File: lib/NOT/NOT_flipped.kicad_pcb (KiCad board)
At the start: 2 copper layers, 2 parts, among them P1 Q_PJFET_GSD

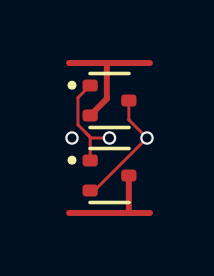
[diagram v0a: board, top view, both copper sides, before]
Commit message: The layout of the NOT gate was also botched (PMOS pinout wrong)
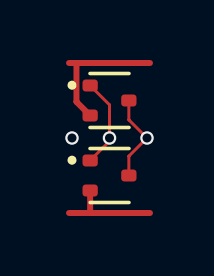
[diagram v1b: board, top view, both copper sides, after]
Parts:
- N1: value Q_NJFET_GSD -> (none)
- P1: value Q_PJFET_GSD -> (none)
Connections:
- P1 pad 2: Y -> VDD
- P1 pad 3: VDD -> Y
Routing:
- net Y: track 4.12 -> 3.00 mm
- net A: track 3.65 -> 3.03 mm
- net VDD: track 3.95 -> 3.45 mm
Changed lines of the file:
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@@
 			)
 		)
-		(property "Value" "Q_PJFET_GSD"
+		(property "Value" ""
 			(at 0 1.75 0)
 			(layer "F.Fab")
@@
 			)
 		)
-		(sheetname "/")
-		(sheetfile "NOT.kicad_sch")
 		(attr smd)
 		(fp_line
@@
 			(net 3 "A")
 			(pinfunction "G")
-			(pintype "input")
+			(pintype "inout")
 		)
 		(pad "2" smd roundrect
@@
 			(layers "F.Cu" "F.Mask" "F.Paste")
 			(roundrect_rratio 0.25)
-			(net 1 "Y")
+			(net 4 "VDD")
 			(pinfunction "S")
-			(pintype "passive")
+			(pintype "inout")
 		)
 		(pad "3" smd roundrect
@@
 			(layers "F.Cu" "F.Mask" "F.Paste")
 			(roundrect_rratio 0.25)
-			(net 4 "VDD")
+			(net 1 "Y")
 			(pinfunction "D")
-			(pintype "passive")
+			(pintype "inout")
 		)
 		(embedded_fonts no)
@@
 			)
 		)
-		(property "Value" "Q_NJFET_GSD"
+		(property "Value" ""
 			(at 0 1.75 0)
 			(layer "F.Fab")
@@
 			)
 		)
-		(sheetname "/")
-		(sheetfile "NOT.kicad_sch")
 		(attr smd)
 		(fp_line
@@
 			(net 3 "A")
 			(pinfunction "G")
-			(pintype "input")
+			(pintype "inout")
 		)
 		(pad "2" smd roundrect
@@
 			(net 2 "GND")
 			(pinfunction "S")
-			(pintype "passive")
+			(pintype "inout")
 		)
 		(pad "3" smd roundrect
@@
 			(net 1 "Y")
 			(pinfunction "D")
-			(pintype "passive")
+			(pintype "inout")
 		)
 		(embedded_fonts no)
@@
 	)
 	(segment
-		(start 0.75 4.25)
-		(end 0.605 4.25)
+		(start 1.895 1.895)
+		(end 2.5 2.5)
+		(width 0.1)
+		(layer "F.Cu")
+		(net 1)
+	)
+	(segment
+		(start 1.895 3.105)
+		(end 1.895 3.75)
 		(width 0.1)
 		(layer "F.Cu")
@@
 	)
 	(segment
-		(start 1.895 1.895)
-		(end 2.5 2.5)
-		(width 0.1)
-		(layer "F.Cu")
-		(net 1)
-	)
-	(segment
 		(start 2.5 2.5)
-		(end 0.75 4.25)
+		(end 1.895 3.105)
 		(width 0.1)
 		(layer "F.Cu")
@@
 	(segment
 		(start -0.1 0)
+		(end 0.2 0)
+		(width 0.2)
+		(layer "F.Cu")
+		(net 2)
+	)
+	(segment
+		(start 0.149 1.294)
+		(end 0.149 0.051)
+		(width 0.2)
+		(layer "F.Cu")
+		(net 2)
+	)
+	(segment
+		(start 0.149 0.051)
+		(end 0.2 0)
+		(width 0.2)
+		(layer "F.Cu")
+		(net 2)
+	)
+	(segment
+		(start 0.605 1.75)
+		(end 0.149 1.294)
+		(width 0.2)
+		(layer "F.Cu")
+		(net 2)
+	)
+	(segment
+		(start 0.2 0)
 		(end 2.6 0)
 		(width 0.2)
@@
 	)
 	(segment
-		(start 1.161 1.194)
-		(end 1.161 0.011)
-		(width 0.2)
-		(layer "F.Cu")
-		(net 2)
-	)
-	(segment
-		(start 0.605 1.75)
-		(end 1.161 1.194)
-		(width 0.2)
-		(layer "F.Cu")
-		(net 2)
-	)
-	(segment
-		(start 1.161 0.011)
-		(end 1.15 0)
-		(width 0.2)
-		(layer "F.Cu")
-		(net 2)
-	)
-	(segment
-		(start 0.199 1.156)
-		(end 0.199 2.061189)
+		(start 1.25 2.5)
+		(end 1.25 2.605)
 		(width 0.1)
 		(layer "F.Cu")
@@
 	)
 	(segment
+		(start 1.25 1.395)
+		(end 1.25 2.5)
+		(width 0.1)
+		(layer "F.Cu")
+		(net 3)
+	)
+	(segment
+		(start 1.25 2.605)
+		(end 0.605 3.25)
+		(width 0.1)
+		(layer "F.Cu")
+		(net 3)
+	)
+	(segment
 		(start 0.605 0.75)
-		(end 0.199 1.156)
-		(width 0.1)
-		(layer "F.Cu")
-		(net 3)
-	)
-	(segment
-		(start 1.25 2.5)
-		(end 0.637812 2.5)
-		(width 0.1)
-		(layer "F.Cu")
-		(net 3)
-	)
-	(segment
-		(start 0.493906 2.356094)
-		(end 0.605 2.467189)
-		(width 0.1)
-		(layer "F.Cu")
-		(net 3)
-	)
-	(segment
-		(start 0.605 2.467189)
-		(end 0.605 3.25)
-		(width 0.1)
-		(layer "F.Cu")
-		(net 3)
-	)
-	(segment
-		(start 0.637812 2.5)
-		(end 0.493906 2.356094)
-		(width 0.1)
-		(layer "F.Cu")
-		(net 3)
-	)
-	(segment
-		(start 0.199 2.061189)
-		(end 0.493906 2.356094)
+		(end 1.25 1.395)
 		(width 0.1)
 		(layer "F.Cu")
@@
 	)
 	(segment
+		(start 0.6 5)
+		(end 2.6 5)
+		(width 0.2)
+		(layer "F.Cu")
+		(net 4)
+	)
+	(segment
+		(start 0.605 4.995)
+		(end 0.6 5)
+		(width 0.2)
+		(layer "F.Cu")
+		(net 4)
+	)
+	(segment
 		(start -0.1 5)
-		(end 2.6 5)
+		(end 0.6 5)
 		(width 0.2)
 		(layer "F.Cu")
@@
 	)
 	(segment
-		(start 1.895 3.75)
-		(end 1.895 4.995)
-		(width 0.2)
-		(layer "F.Cu")
-		(net 4)
-	)
-	(segment
-		(start 1.895 4.995)
-		(end 1.9 5)
-		(width 0.2)
-		(layer "F.Cu")
+		(start 0.605 4.25)
+		(end 0.605 4.995)
+		(width 0.2)
+		(layer "F.Cu")

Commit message: High-density layout with pitch of 1.1mm, which gains 23% !!
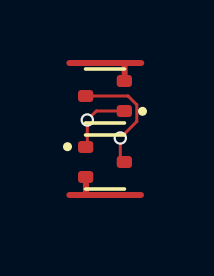
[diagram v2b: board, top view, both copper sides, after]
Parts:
- moved P1 0.47 mm to (1.10, 3.30)
- moved N1 0.21 mm to (1.10, 1.10), turned to 180 degrees
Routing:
- net GND: track 4.66 -> 3.00 mm
- net Y: track 3.00 -> 4.01 mm
- net A: track 3.03 -> 2.29 mm
- net (no net): vias 1 -> 0

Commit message: All cells now use 1mm*4mm grid rather than 1.1mm*4.4mm
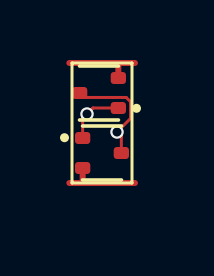
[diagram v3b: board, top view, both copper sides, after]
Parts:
- moved P1 0.32 mm to (1.00, 3.00)
- moved N1 0.22 mm to (0.90, 1.00)
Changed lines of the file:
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@@
 	(footprint "Package_TO_SOT_SMD:SOT-523"
 		(layer "F.Cu")
-		(at 1.1 1.1 180)
+		(at 0.9 1 180)
 		(descr "SOT523, https://www.diodes.com/assets/Package-Files/SOT523.pdf")
 		(tags "SOT-523")
@@
 	(footprint "Package_TO_SOT_SMD:SOT-523"
 		(layer "F.Cu")
-		(at 1.1 3.3)
+		(at 1 3)
 		(descr "SOT523, https://www.diodes.com/assets/Package-Files/SOT523.pdf")
 		(tags "SOT-523")
@@
 		)
 	)
-	(segment
-		(start 1.61 2.5)
-		(end 1.61 3.155)
-		(width 0.1)
-		(layer "F.Cu")
-		(net 1)
-	)
-	(segment
-		(start 2.161 1.393262)
-		(end 2.161 1.949)
-		(width 0.1)
-		(layer "F.Cu")
-		(net 1)
-	)
-	(segment
-		(start 0.465 1.1)
-		(end 1.867738 1.1)
-		(width 0.1)
-		(layer "F.Cu")
-		(net 1)
-	)
-	(segment
-		(start 1.867738 1.1)
-		(end 2.161 1.393262)
-		(width 0.1)
-		(layer "F.Cu")
-		(net 1)
-	)
-	(segment
-		(start 1.61 3.155)
-		(end 1.755 3.3)
-		(width 0.1)
-		(layer "F.Cu")
-		(net 1)
-	)
-	(segment
-		(start 2.161 1.949)
-		(end 1.61 2.5)
+	(gr_rect
+		(start 0 0)
+		(end 2 4)
+		(stroke
+			(width 0.1)
+			(type default)
+		)
+		(fill no)
+		(layer "F.SilkS")
+	)
+	(segment
+		(start 1.645 2.445)
+		(end 1.5 2.3)
+		(width 0.1)
+		(layer "F.Cu")
+		(net 1)
+	)
+	(segment
+		(start 1.951 1.293262)
+		(end 1.951 1.849)
+		(width 0.1)
+		(layer "F.Cu")
+		(net 1)
+	)
+	(segment
+		(start 0.255 1)
+		(end 0.404 1.149)
+		(width 0.1)
+		(layer "F.Cu")
+		(net 1)
+	)
+	(segment
+		(start 1.645 3)
+		(end 1.645 2.445)
+		(width 0.1)
+		(layer "F.Cu")
+		(net 1)
+	)
+	(segment
+		(start 0.404 1.149)
+		(end 1.806738 1.149)
+		(width 0.1)
+		(layer "F.Cu")
+		(net 1)
+	)
+	(segment
+		(start 1.951 1.849)
+		(end 1.5 2.3)
+		(width 0.1)
+		(layer "F.Cu")
+		(net 1)
+	)
+	(segment
+		(start 1.806738 1.149)
+		(end 1.951 1.293262)
 		(width 0.1)
 		(layer "F.Cu")
@@
 	)
 	(via
-		(at 1.61 2.5)
+		(at 1.5 2.3)
 		(size 0.45)
 		(drill 0.3)
@@
 	)
 	(segment
-		(start 1.755 0.6)
-		(end 1.755 0.005)
+		(start 1.545 0.5)
+		(end 1.545 0.045)
 		(width 0.2)
 		(layer "F.Cu")
@@
 	(segment
 		(start 1.76 0)
-		(end 2.31 0)
+		(end 2.1 0)
 		(width 0.2)
 		(layer "F.Cu")
@@
 	(segment
 		(start -0.09 0)
+		(end 1.5 0)
+		(width 0.2)
+		(layer "F.Cu")
+		(net 2)
+	)
+	(segment
+		(start 1.545 0.045)
+		(end 1.5 0)
+		(width 0.2)
+		(layer "F.Cu")
+		(net 2)
+	)
+	(segment
+		(start 1.5 0)
 		(end 1.76 0)
 		(width 0.2)
@@
 	)
 	(segment
-		(start 0.81 1.6)
-		(end 0.51 1.9)
+		(start 0.355 2.5)
+		(end 0.355 1.845)
 		(width 0.1)
 		(layer "F.Cu")
@@
 	)
 	(segment
-		(start 1.755 1.6)
-		(end 0.81 1.6)
+		(start 1.545 1.5)
+		(end 0.7 1.5)
 		(width 0.1)
 		(layer "F.Cu")
@@
 	)
 	(segment
-		(start 0.51 2.755)
-		(end 0.465 2.8)
+		(start 0.355 1.845)
+		(end 0.5 1.7)
 		(width 0.1)
 		(layer "F.Cu")
@@
 	)
 	(segment
-		(start 0.51 1.9)
-		(end 0.51 2.755)
+		(start 0.7 1.5)
+		(end 0.5 1.7)
 		(width 0.1)
 		(layer "F.Cu")
@@
 	)
 	(via
-		(at 0.51 1.9)
+		(at 0.5 1.7)
 		(size 0.45)
 		(drill 0.3)
@@
 	)
 	(segment
-		(start 0.45 4.4)
-		(end -0.09 4.4)
+		(start 0.3 4)
+		(end -0.09 4)
 		(width 0.2)
 		(layer "F.Cu")
@@
 	)
 	(segment
-		(start 0.615 4.4)
-		(end 2.3 4.4)
+		(start 0.45 4)
+		(end 0.3 4)
 		(width 0.2)
 		(layer "F.Cu")
@@
 	)
 	(segment
-		(start 0.61 4.4)
-		(end 0.45 4.4)
+		(start 0.615 4)
+		(end 2.1 4)
 		(width 0.2)
 		(layer "F.Cu")
@@
 	)
 	(segment
-		(start 0.465 4.385)
-		(end 0.45 4.4)
+		(start 0.355 3.5)
+		(end 0.355 3.945)
 		(width 0.2)
 		(layer "F.Cu")
@@
 	)
 	(segment
-		(start 0.465 3.8)
-		(end 0.465 4.385)
-		(width 0.2)
-		(layer "F.Cu")
+		(start 0.61 4)
+		(end 0.45 4)
+		(width 0.2)
+		(layer "F.Cu")
+		(net 4)
+	)
+	(segment
+		(start 0.465 4)
+		(end 0.45 4)
+		(width 0.2)
+		(layer "F.Cu")
+		(net 4)
+	)
+	(segment
+		(start 0.355 3.945)
+		(end 0.3 4)
+		(width 0.2)
+		(layer "F.Cu")

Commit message: Make the pads of my SOT523 footprint very slightly smaller, which is enough to route all the cells and leave the mosfets exactly on the grid
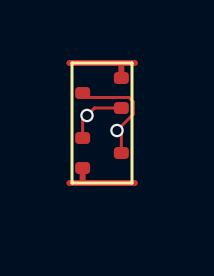
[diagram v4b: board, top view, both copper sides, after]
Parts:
- N1, P1: footprint Package_TO_SOT_SMD:SOT-523 -> RV523:SOT523
- moved N1 0.10 mm to (1.00, 1.00)

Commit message: Propagate MOSFET values to the cells' PCBs
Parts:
- N1: value (none) -> NMOS
- P1: value (none) -> PMOS
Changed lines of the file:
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@@
 			)
 		)
-		(property "Value" ""
+		(property "Value" "NMOS"
 			(at 0 0 180)
 			(layer "F.Fab")
@@
 			)
 		)
-		(property "Value" ""
+		(property "Value" "PMOS"
 			(at 0 0 0)
 			(layer "F.Fab")
